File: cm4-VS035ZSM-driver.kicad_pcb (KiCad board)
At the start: 4 copper layers, 70 x 50 mm, 75 parts, among them J1 Conn_01x22, J2 245863050104829+, U1 MCP1603T-180I/OS, U2 LP3320B6F, U3 TPS65132WRVCR_C2876379, U4 KF1027B-04P-G00-DFT-01B, U5 KF1027B-04P-G00-DFT-01B, U6 PZ254-2-08-WS

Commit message: done with v2
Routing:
- net LED_PWM: track 48.6 -> 46.9 mm
- net /LED_PWR.K: vias 5 -> 4
- net +5V_IN: vias 22 -> 18
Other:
- outline, holes or cut-outs redrawn
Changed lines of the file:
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@@
 		(tags "XF2M-2215-1A ")
 		(property "Reference" "J1"
-			(at 0 2.4511 0)
+			(at 7.19 3.9911 0)
 			(unlocked yes)
 			(layer "F.SilkS")
@@
 		(layer "Dwgs.User")
 	)
-	(gr_rect
-		(start 99.3 82.3)
-		(end 169.3 132.3)
+	(gr_arc
+		(start 99.3 87.3)
+		(mid 100.764466 83.764466)
+		(end 104.3 82.3)
 		(stroke
 			(width 0.2)
-			(type solid)
+			(type default)
+		)
+		(layer "Edge.Cuts")
+	)
+	(gr_line
+		(start 99.3 127.3)
+		(end 99.3 87.3)
+		(stroke
+			(width 0.2)
+			(type default)
+		)
+		(layer "Edge.Cuts")
+	)
+	(gr_line
+		(start 104.3 82.3)
+		(end 164.3 82.3)
+		(stroke
+			(width 0.2)
+			(type default)
+		)
+		(layer "Edge.Cuts")
+	)
+	(gr_arc
+		(start 104.3 132.3)
+		(mid 100.764466 130.835534)
+		(end 99.3 127.3)
+		(stroke
+			(width 0.2)
+			(type default)
+		)
+		(layer "Edge.Cuts")
+	)
+	(gr_arc
+		(start 164.3 82.3)
+		(mid 167.835534 83.764466)
+		(end 169.3 87.3)
+		(stroke
+			(width 0.2)
+			(type default)
+		)
+		(layer "Edge.Cuts")
+	)
+	(gr_line
+		(start 164.3 132.3)
+		(end 104.3 132.3)
+		(stroke
+			(width 0.2)
+			(type default)
+		)
+		(layer "Edge.Cuts")
+	)
+	(gr_line
+		(start 169.3 87.3)
+		(end 169.3 127.3)
+		(stroke
+			(width 0.2)
+			(type default)
+		)
+		(layer "Edge.Cuts")
+	)
+	(gr_arc
+		(start 169.3 127.3)
+		(mid 167.835534 130.835534)
+		(end 164.3 132.3)
+		(stroke
+			(width 0.2)
+			(type default)
 		)
-		(fill no)
 		(layer "Edge.Cuts")
 	)
@@
 		)
 	)
-	(gr_text "good luck!"
-		(at 101.44 116.42 90)
+	(gr_text "hello! hello! hello!"
+		(at 184.98 111.17 0)
 		(layer "F.SilkS")
 		(effects
 			(font
-				(size 0.9 1)
+				(size 1 1)
 				(thickness 0.15)
 			)
@@
 		)
 	)
-	(gr_text "hello! hello! hello!"
-		(at 184.98 111.17 0)
+	(gr_text "VS035ZSM MIPI Driver\nBy Vincent Xie"
+		(at 149.04 85.86 0)
 		(layer "F.SilkS")
 		(effects
@@
 				(size 1 1)
 				(thickness 0.15)
+				(bold yes)
 			)
 			(justify left bottom)
 		)
 	)
-	(gr_text "VS035ZSM MIPI Driver\nBy Vincent Xie"
-		(at 149.04 85.86 0)
+	(gr_text "good luck!"
+		(at 101.64 116.43 90)
 		(layer "F.SilkS")
 		(effects
@@
 				(size 1 1)
 				(thickness 0.15)
-				(bold yes)
 			)
 			(justify left bottom)
@@
 	)
 	(segment
-		(start 137.47 115.52)
+		(start 136.825 114.635)
 		(end 137.47 113.99)
 		(width 0.15)
@@
 	)
 	(segment
-		(start 114.399999 87.7)
-		(end 114.399999 86.820001)
+		(start 136.585 114.635)
+		(end 136.825 114.635)
 		(width 0.15)
 		(layer "F.Cu")
@@
 	)
 	(segment
-		(start 137.49 115.54)
-		(end 137.47 115.52)
+		(start 114.399999 87.7)
+		(end 114.399999 86.820001)
 		(width 0.15)
 		(layer "F.Cu")
@@
 	)
 	(via
-		(at 137.49 115.54)
+		(at 136.585 114.635)
 		(size 0.45)
 		(drill 0.3)
@@
 	)
 	(segment
-		(start 130.98 97.05)
+		(start 136.585 114.635)
 		(end 130.98 109.03)
 		(width 0.15)
@@
 	(segment
 		(start 130.98 109.03)
-		(end 137.49 115.54)
+		(end 130.98 97.05)
 		(width 0.15)
 		(layer "B.Cu")
@@
 	)
 	(via
-		(at 133.79 103.29)
-		(size 0.45)
-		(drill 0.3)
-		(layers "F.Cu" "B.Cu")
-		(free yes)
-		(net "+5V_IN")
-	)
-	(via
-		(at 135.63 102.6)
+		(at 135.74 103.02)
 		(size 0.45)
 		(drill 0.3)
@@
 	)
 	(via
-		(at 136.06 103.28)
-		(size 0.45)
-		(drill 0.3)
-		(layers "F.Cu" "B.Cu")
-		(free yes)
-		(net "+5V_IN")
-	)
-	(via
-		(at 134.54 101.94)
+		(at 134.47 102.25)
 		(size 0.45)
 		(drill 0.3)
@@
 	)
 	(via
-		(at 134.92 102.59)
+		(at 134.94 103.06)
 		(size 0.45)
 		(drill 0.3)
@@
 	)
 	(via
-		(at 135.29 101.93)
-		(size 0.45)
-		(drill 0.3)
-		(layers "F.Cu" "B.Cu")
-		(free yes)
-		(net "+5V_IN")
-	)
-	(via
-		(at 134.52 103.28)
+		(at 135.38 102.22)
 		(size 0.45)
 		(drill 0.3)
@@
 	)
 	(via
-		(at 135.3 103.28)
-		(size 0.45)
-		(drill 0.3)
-		(layers "F.Cu" "B.Cu")
-		(free yes)
-		(net "+5V_IN")
-	)
-	(via
-		(at 134.18 102.6)
+		(at 133.9 103.09)
 		(size 0.45)
 		(drill 0.3)
@@
 	)
 	(via
-		(at 129.8 109.15)
-		(size 0.45)
-		(drill 0.3)
-		(layers "F.Cu" "B.Cu")
-		(net "/LED_PWR.K")
-	)
-	(via
 		(at 133.55 112.9)
 		(size 0.45)
@@
 	)
 	(segment
+		(start 104.37 108.1)
+		(end 104.72 108.45)
+		(width 0.15)
+		(layer "F.Cu")
+		(net "LCD_CONNECTOR_PWM")
+	)
+	(segment
 		(start 142.559995 94.5)
 		(end 142.559995 92.619995)
@@
 	)
 	(segment
-		(start 104.54 108.27)
-		(end 104.72 108.45)
+		(start 104.37 108.02)
+		(end 104.37 108.1)
 		(width 0.15)
 		(layer "F.Cu")
@@
 	)
 	(via
-		(at 104.54 108.27)
+		(at 104.37 108.02)
 		(size 0.45)
 		(drill 0.3)
@@
 	)
 	(segment
-		(start 110.97 85.72)
-		(end 104.37 92.32)
-		(width 0.15)
-		(layer "B.Cu")
-		(net "LCD_CONNECTOR_PWM")
-	)
-	(segment
-		(start 141.68 91.74)
-		(end 135.66 85.72)
+		(start 135.66 85.72)
+		(end 141.68 91.74)
 		(width 0.15)
 		(layer "B.Cu")
@@
 	(segment
 		(start 104.37 92.32)
-		(end 104.37 108.1)
+		(end 110.97 85.72)
 		(width 0.15)
 		(layer "B.Cu")
@@
 	)
 	(segment
-		(start 135.66 85.72)
-		(end 110.97 85.72)
+		(start 104.37 108.02)
+		(end 104.37 92.32)
 		(width 0.15)
 		(layer "B.Cu")
@@
 	)
 	(segment
-		(start 104.37 108.1)
-		(end 104.54 108.27)
+		(start 110.97 85.72)
+		(end 135.66 85.72)
 		(width 0.15)
 		(layer "B.Cu")
@@
 	)
 	(segment
-		(start 105.4 109.15)
-		(end 104.58 109.15)
+		(start 104.82 109.15)
+		(end 105.4 109.15)
 		(width 0.15)
 		(layer "F.Cu")
@@
 	)
 	(segment
-		(start 131.55 94.5)
-		(end 132.399974 94.5)
+		(start 104.61 108.94)
+		(end 104.82 109.15)
 		(width 0.15)
 		(layer "F.Cu")
@@
 	)
 	(segment
-		(start 104.58 109.15)
-		(end 104.37 108.94)
+		(start 131.55 94.5)
+		(end 132.399974 94.5)
 		(width 0.15)
 		(layer "F.Cu")
@@
 	)
 	(via
-		(at 104.37 108.94)
+		(at 104.61 108.94)
 		(size 0.45)
 		(drill 0.3)
@@
 	)
 	(segment
-		(start 126.83 99.22)
-		(end 131.06 94.99)
+		(start 105.48 108.94)
+		(end 115.2 99.22)
 		(width 0.15)
 		(layer "B.Cu")
@@
 	)
 	(segment
-		(start 115.2 99.22)
-		(end 126.83 99.22)
+		(start 126.83 99.22)
+		(end 131.06 94.99)
 		(width 0.15)
 		(layer "B.Cu")
@@
 	)
 	(segment
-		(start 105.48 108.94)
-		(end 115.2 99.22)
+		(start 104.61 108.94)
+		(end 105.48 108.94)
 		(width 0.15)
 		(layer "B.Cu")
@@
 	)
 	(segment
-		(start 104.37 108.94)
-		(end 105.48 108.94)
+		(start 115.2 99.22)
+		(end 126.83 99.22)
 		(width 0.15)
 		(layer "B.Cu")

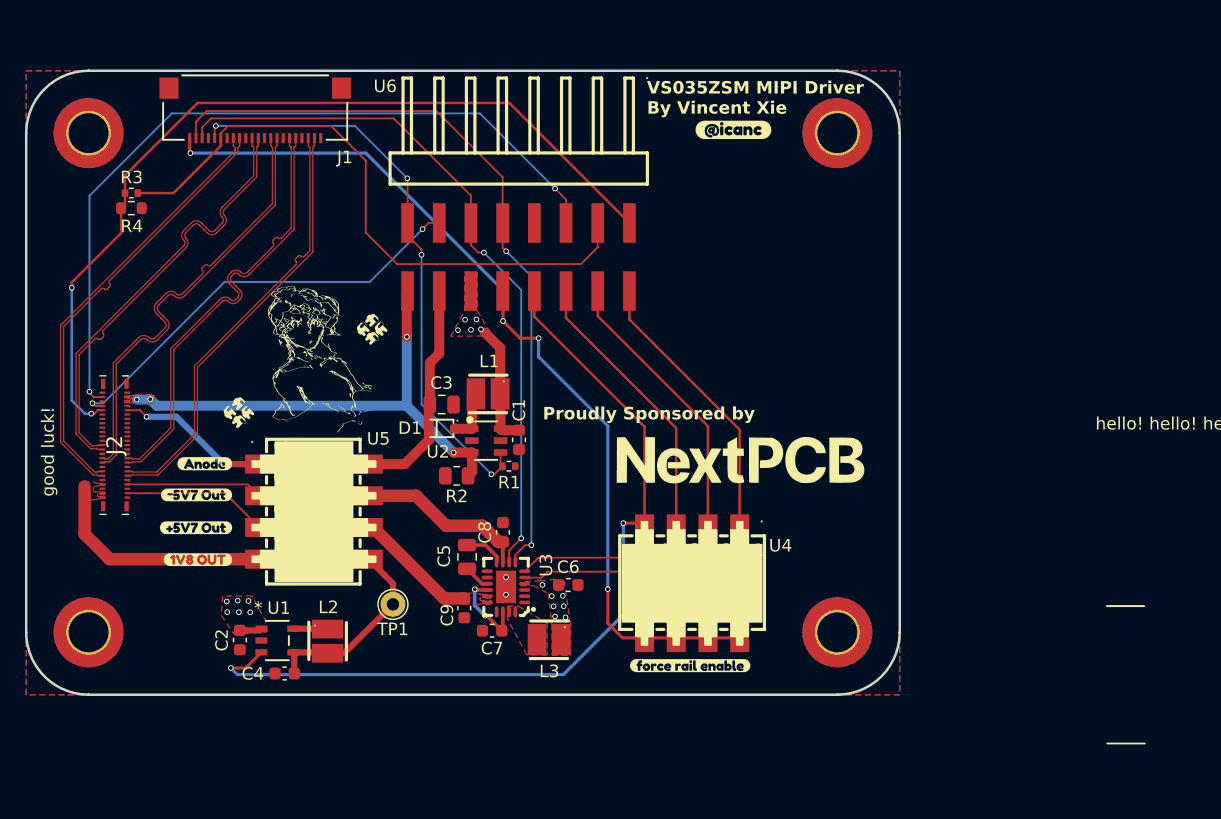
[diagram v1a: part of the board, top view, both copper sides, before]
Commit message: swap J2 connector to full-pads variant and use vias for routing
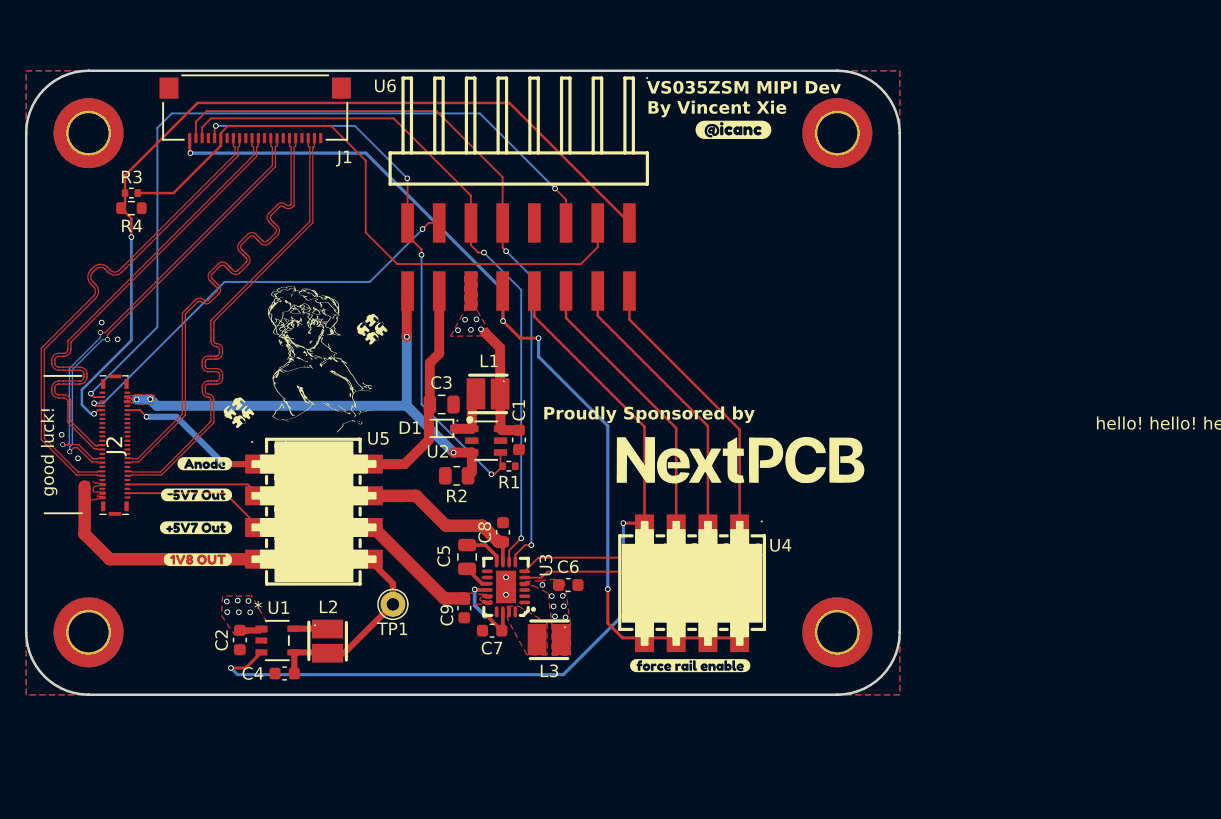
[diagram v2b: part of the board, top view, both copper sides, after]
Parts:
- J2: footprint footprints:245863050104829_missing pads -> footprints:245863050104829
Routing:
- net /DSI0_DATA.2_N: track 34.6 -> 38.7 mm
- net /DSI0_DATA.3_N: track 34.7 -> 38.8 mm
- net /DSI0_DATA.0_N: track 34.7 -> 38.7 mm
- net /DSI0_DATA.1_N: track 34.6 -> 38.6 mm
- net /DSI0_DATA.2_P: track 34.5 -> 38.3 mm
- net /DSI0_DATA.3_P: track 34.6 -> 38.4 mm
- net /DSI0_DATA.0_P: track 34.6 -> 38.3 mm
- net /DSI0_DATA.1_P: track 34.5 -> 38.2 mm
- net /DSI0_CLK.P: track 34.5 -> 35.7 mm, vias 0 -> 2
- net /DSI0_CLK.N: track 34.6 -> 35.5 mm, vias 0 -> 2
- net GND: vias 2 -> 6
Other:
- board text added: "VS035ZSM MIPI Dev By Vincent Xie"
- board text removed: "VS035ZSM MIPI Driver By Vincent Xie"

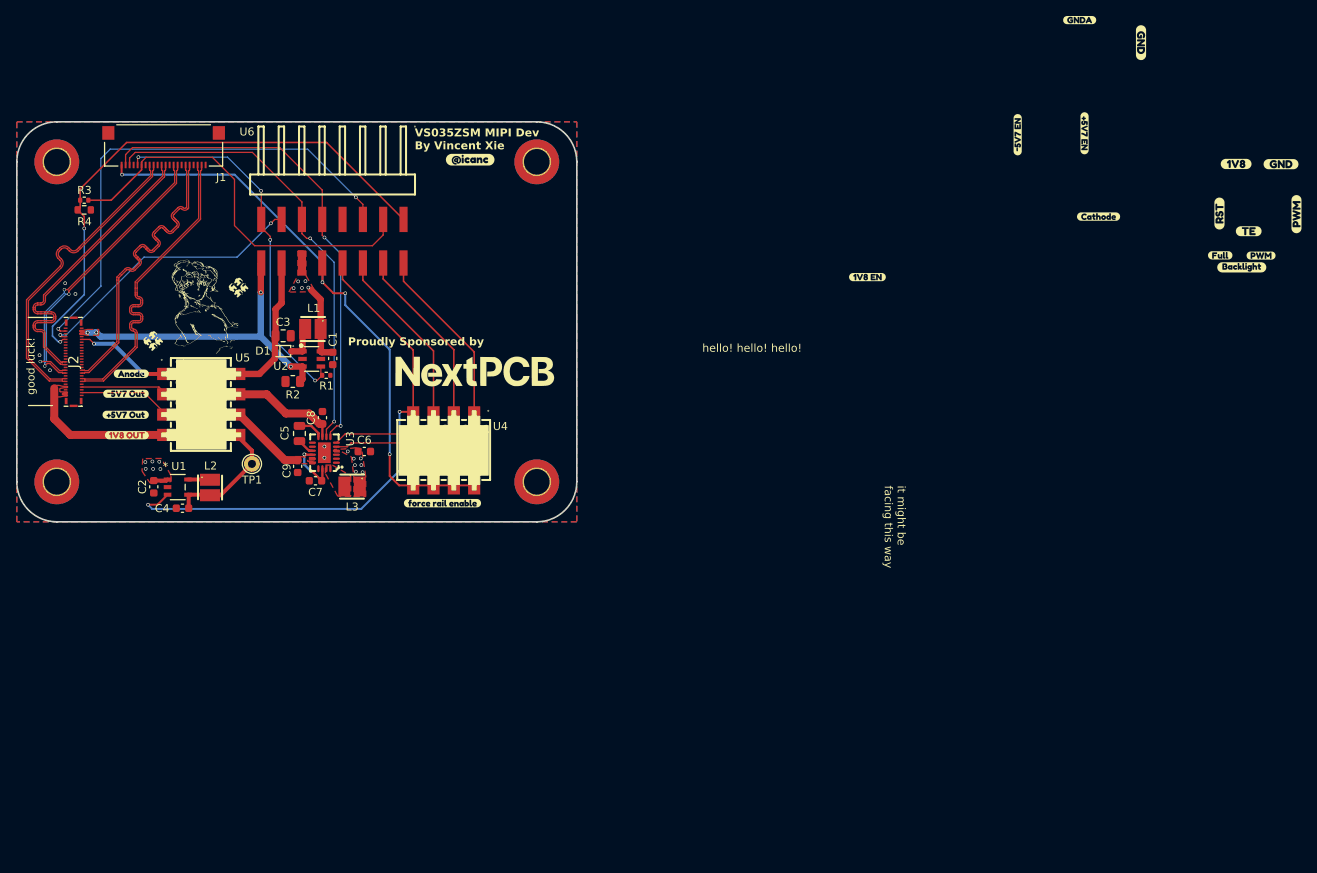
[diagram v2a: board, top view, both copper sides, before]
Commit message: update PCB, add design review notes + analysis dir
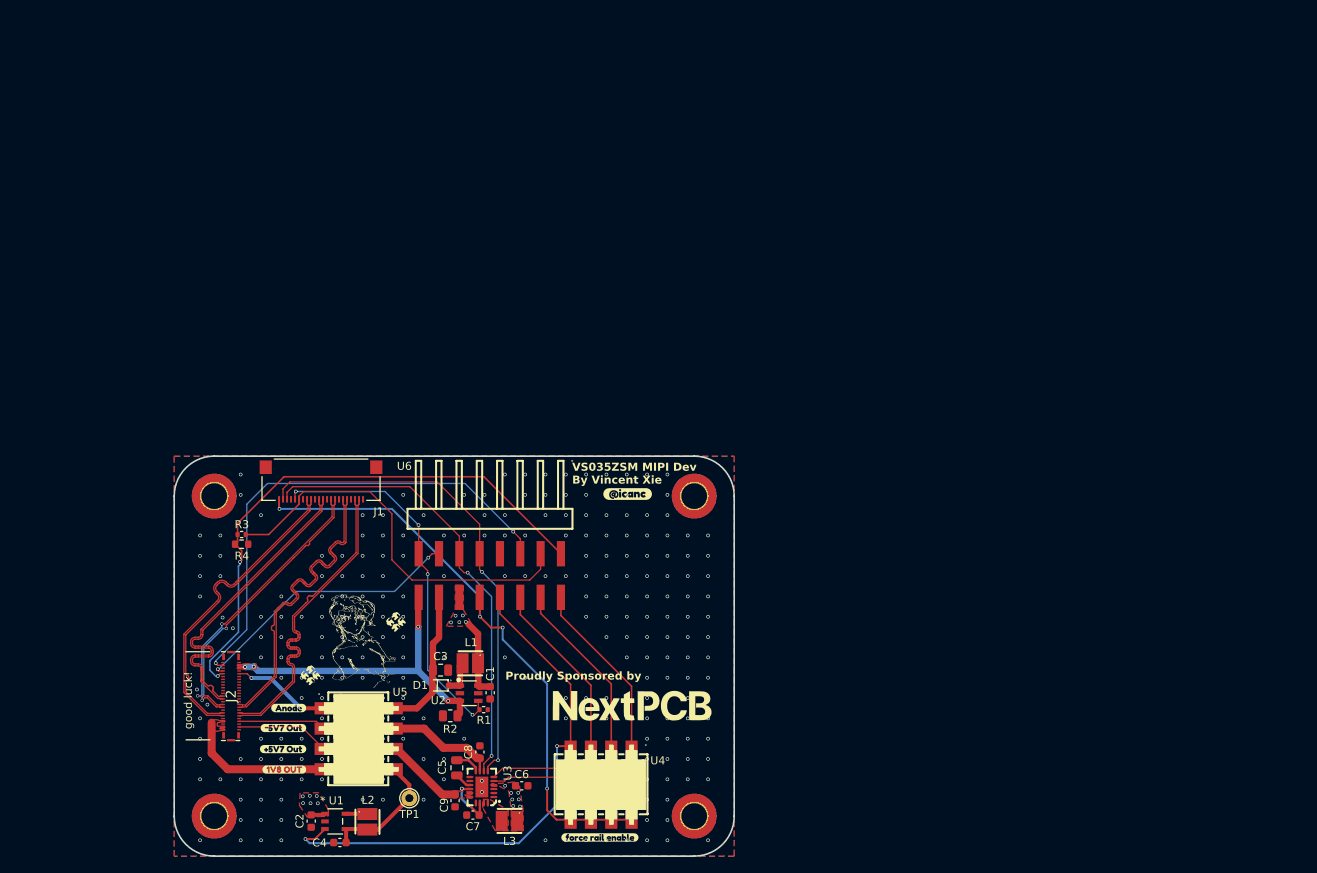
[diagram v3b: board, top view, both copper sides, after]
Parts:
- removed kibuzzard-685CA5E3 (x2): G***, kibuzzard-685CA5E3
- removed the kibuzzard-685CA5ED at (227.6, 132.8)
- removed kibuzzard-685CA646 (x2): G***, kibuzzard-685CA646
- removed kibuzzard-685CA653 (x2): G***, kibuzzard-685CA653
- removed kibuzzard-685CA659 (x2): G***, kibuzzard-685CA659
- removed kibuzzard-685CA68D (x2): G***, kibuzzard-685CA68D
- removed kibuzzard-685CA698 (x2): G***, kibuzzard-685CA698
- removed the kibuzzard-685CA6CA at (233.5, 126.0)
- removed the kibuzzard-685CA6D3 at (230.6, 115.2)
- removed kibuzzard-685CA6E7 (x2): G***, kibuzzard-685CA6E7
- removed kibuzzard-685CA70B: G***, kibuzzard-685CA70B
- removed the kibuzzard-685CA724 at (244.1, 115.7)
- removed kibuzzard-685CA72C (x2): G***, kibuzzard-685CA72C
- removed kibuzzard-68620294 (x2): G***, kibuzzard-68620294
- removed kibuzzard-686202AB (x4): G***, kibuzzard-686202AB
- removed kibuzzard-686202C6 (x2): G***, kibuzzard-686202C6
- removed kibuzzard-686202CD (x2): G***, kibuzzard-686202CD
- removed kibuzzard-68621440 (x2): G***, kibuzzard-68621440
- removed kibuzzard-68622B0B: G***, kibuzzard-68622B0B
- removed kibuzzard-68622B1B: G***, kibuzzard-68622B1B
- moved R1 46.2 mm to (157.7, 155.8)
- moved H1 46.2 mm to (124.0, 129.1)
- moved H4 46.2 mm to (124.0, 169.1)
- moved J2 46.2 mm to (126.1, 154.1)
- moved C2 46.2 mm to (136.1, 169.7)
- moved C3 46.2 mm to (152.3, 150.8)
- moved C5 46.2 mm to (154.3, 163.0)
- moved C6 46.2 mm to (162.4, 165.3)
- moved C7 46.2 mm to (156.3, 169.0)
- moved C8 46.2 mm to (157.2, 161.1)
- moved C9 46.2 mm to (154.1, 167.1)
- moved D1 46.2 mm to (152.3, 152.7)
- moved H2 46.2 mm to (184.0, 129.1)
- moved H3 46.2 mm to (184.0, 169.1)
- moved L3 46.2 mm to (160.9, 169.7)
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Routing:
- net GND: vias 6 -> 264
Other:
- board text removed: "hello! hello! hello!"
- board text removed: "it might be facing this way"
